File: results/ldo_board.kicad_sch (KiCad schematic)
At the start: 7 parts, among them J1 2-pin connector, J2 Conn_01x02, U1 LP38693DT-3.3

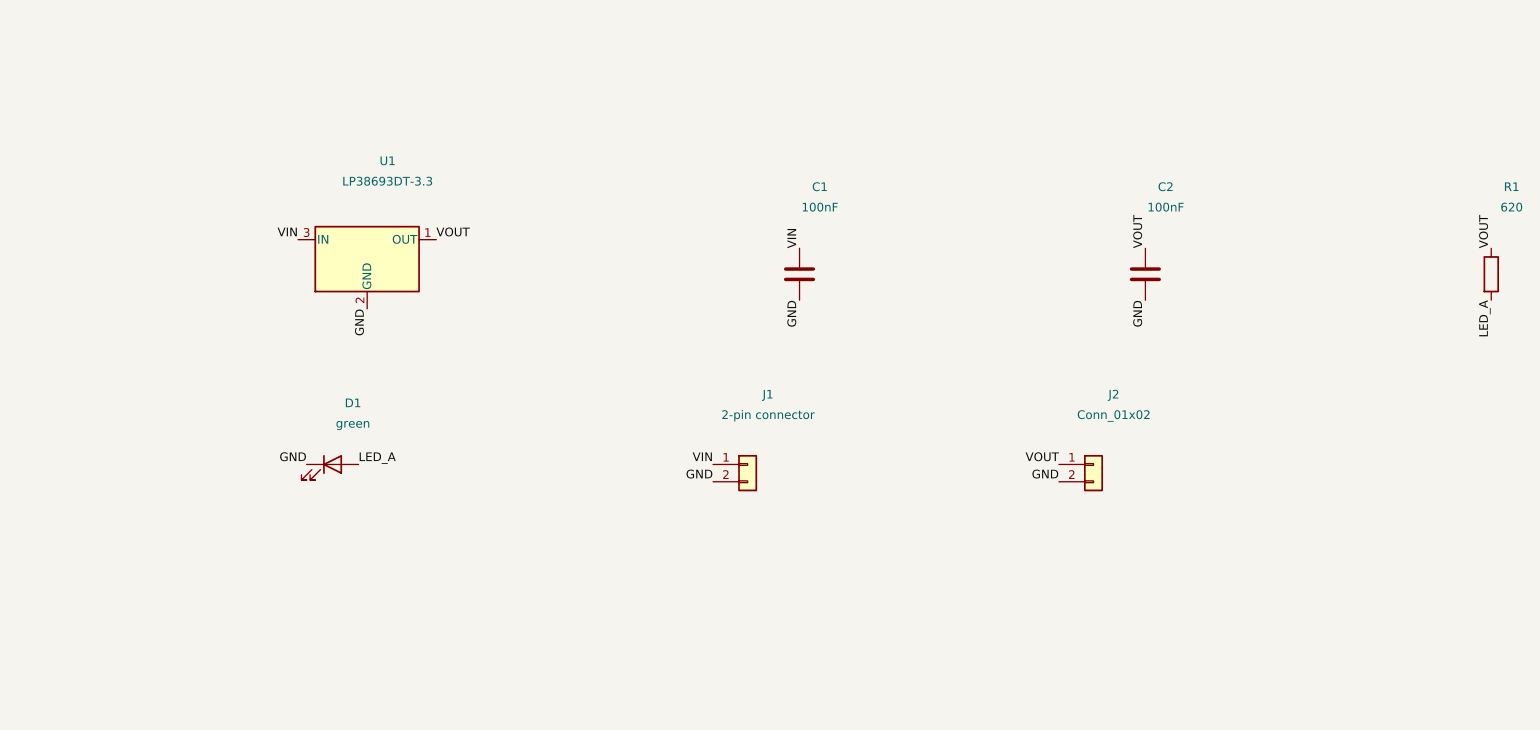
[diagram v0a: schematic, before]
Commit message: Draw schematics with real wires, verified against KiCad's netlist
- schematic.py: parts in columns along the signal flow, one vertical bar per
  net, every pin wired; layout variants are tried until KiCad's own netlist
  export reads back exactly our nets, otherwise the label style is used.
  Also writes a minimal .kicad_pro so the file opens in KiCad.
- datasheet part cards: read 40 pages with several targeted queries, new
  min input/output capacitance fields and lint rule E054 (found with the LP38693
  LDO whose datasheet asks for >= 1 uF while the model used 100 nF).
- tests: 62.

Co-Authored-By: Claude Sonnet 5.5 <noreply@anthropic.com>
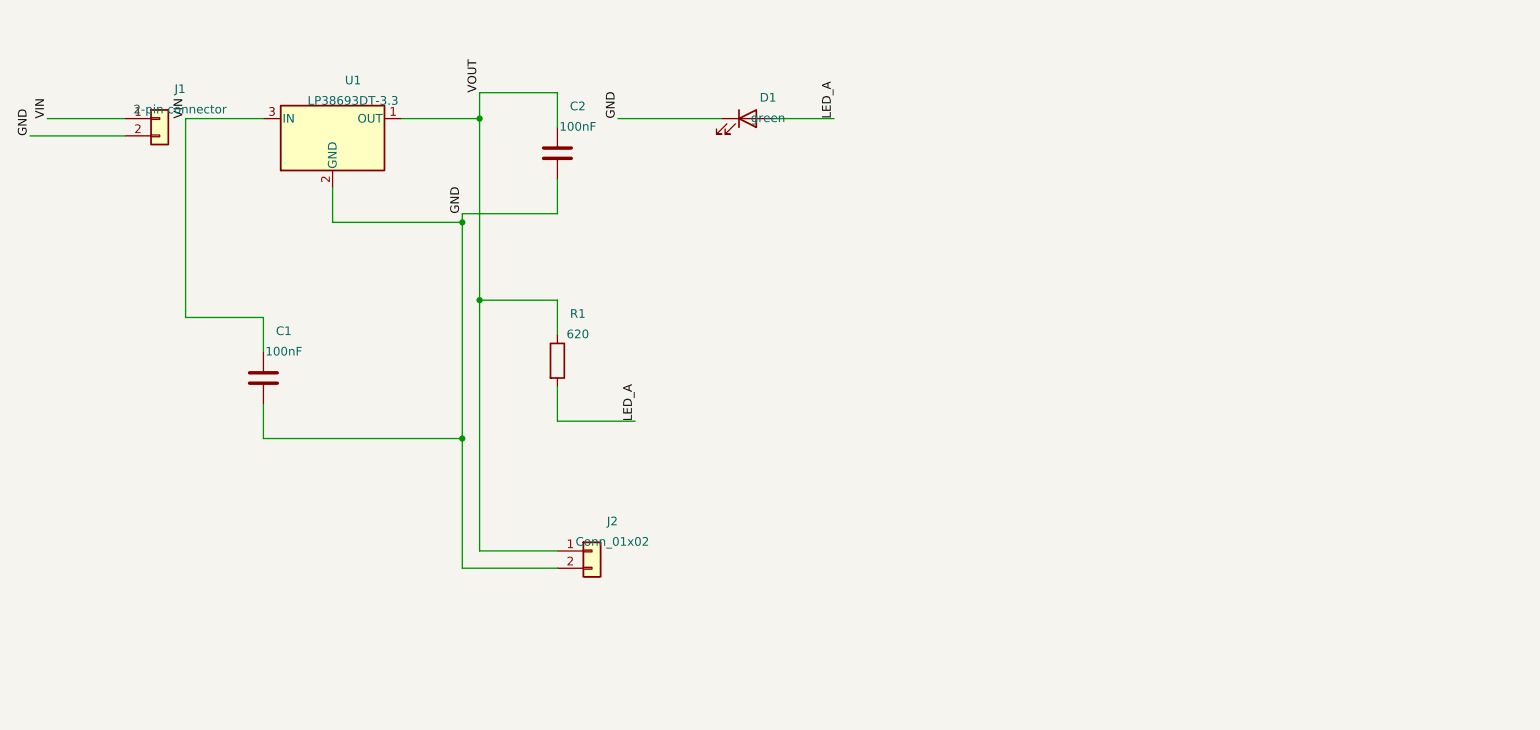
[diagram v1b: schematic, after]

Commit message: Join nets that span several columns with a bridge wire
Every net is now fully wired in the schematic (GND as one central bar), each
drawing is checked against KiCad's own netlist export and layout variants are
tried until it matches.

Co-Authored-By: Claude Sonnet 5.5 <noreply@anthropic.com>
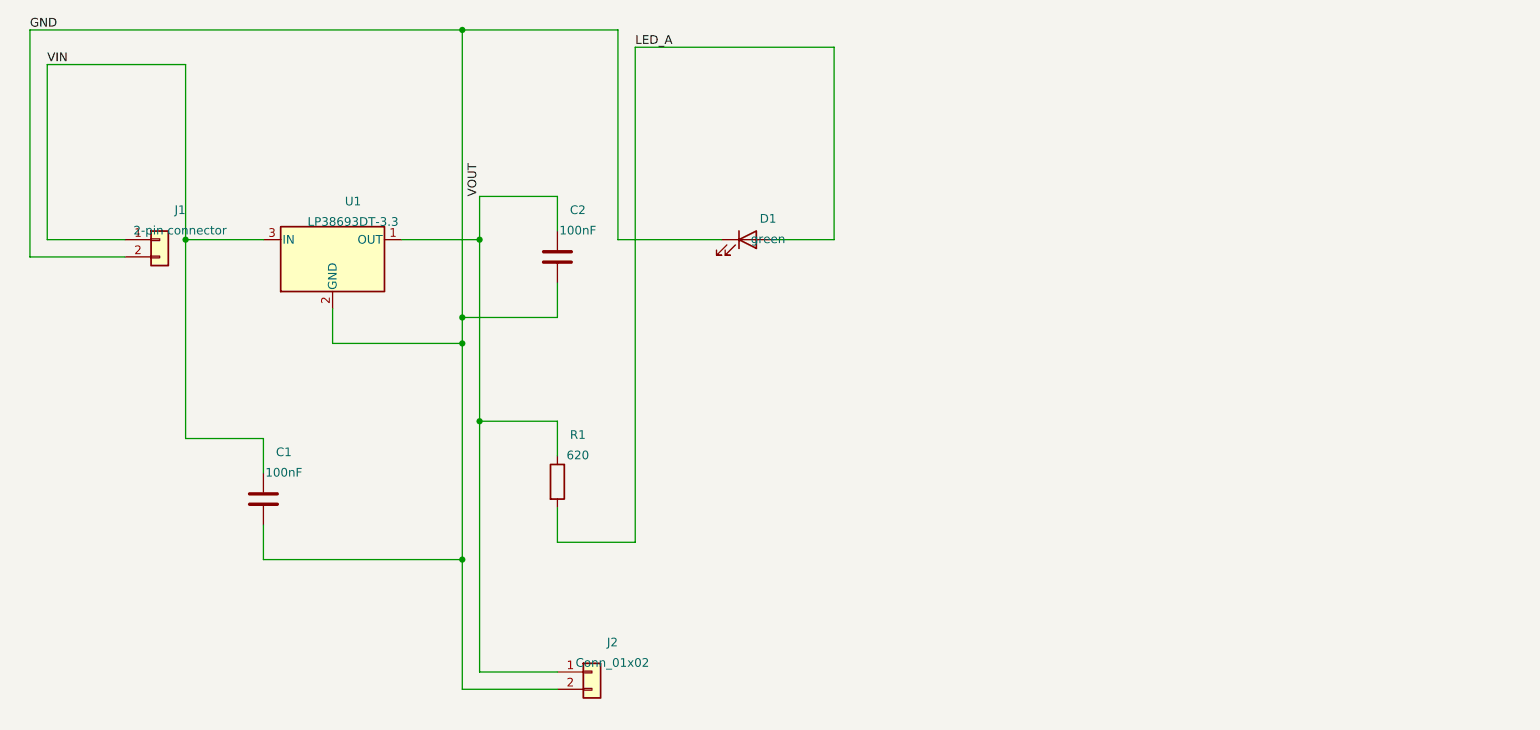
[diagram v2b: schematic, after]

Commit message: Cleaner schematics: KiCad power symbols for rails and GND, wires only for signals
Rails and ground are drawn with standard power symbols (net name as value) so the
long GND/supply bars and bridge wires disappear; only signal nets are wired.
Part and symbol texts sit beside the symbols and channels are wider. Every
drawing is still verified against KiCad's own netlist, falling back to the
wires-only and label styles if a layout does not verify.

Co-Authored-By: Claude Sonnet 5.5 <noreply@anthropic.com>
Claude-Session: https://claude.ai/code/session_01FMm5QrTg7cbs2KFpDvJyj1
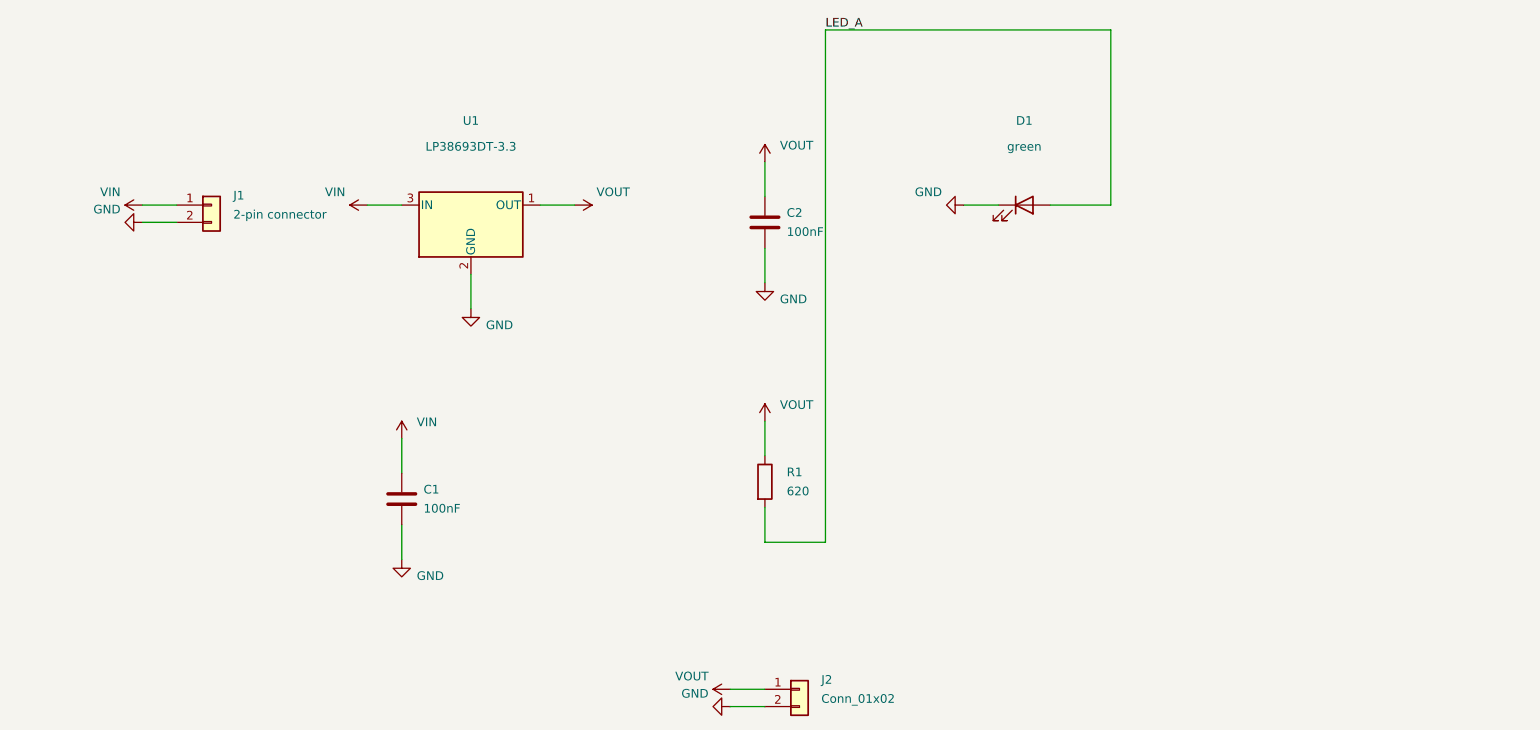
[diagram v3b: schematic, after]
